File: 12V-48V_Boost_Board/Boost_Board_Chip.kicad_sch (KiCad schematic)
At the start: 22 parts, among them Q1 100V

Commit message: Implemented feedback from request
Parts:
- L1: footprint Inductor_SMD:L_0805_2012Metric_Pad1.05x1.20mm_HandSolder -> Library:WE-HCF_SMD_HIGH-CURRENT_INDUCTOR
- R4: value 1000Ω -> 1kΩ
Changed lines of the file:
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@@
 	(wire
 		(pts
-			(xy 30.48 60.96) (xy 43.18 60.96)
+			(xy 38.1 60.96) (xy 43.18 60.96)
 		)
 		(stroke
@@
 	(wire
 		(pts
-			(xy 30.48 60.96) (xy 30.48 110.49)
-		)
-		(stroke
-			(width 0)
-			(type default)
-		)
-	)
-	(wire
-		(pts
 			(xy 152.4 121.92) (xy 152.4 128.27)
 		)
@@
 	(wire
 		(pts
-			(xy 265.43 60.96) (xy 265.43 110.49)
-		)
-		(stroke
-			(width 0)
-			(type default)
-		)
-	)
-	(wire
-		(pts
 			(xy 166.37 93.98) (xy 166.37 124.46)
 		)
@@
 	(wire
 		(pts
-			(xy 246.38 60.96) (xy 265.43 60.96)
+			(xy 246.38 60.96) (xy 254 60.96)
 		)
 		(stroke
@@
 	(hierarchical_label "12V_INPUT"
 		(shape output)
-		(at 30.48 110.49 180)
+		(at 38.1 60.96 180)
 		(fields_autoplaced yes)
 		(effects
@@
 	(hierarchical_label "48V_OUTPUT"
 		(shape input)
-		(at 265.43 110.49 0)
+		(at 254 60.96 0)
 		(fields_autoplaced yes)
 		(effects
@@
 			)
 		)
-		(property "Datasheet" ""
+		(property "Datasheet" "https://www.ti.com/lit/ds/symlink/lm5156h.pdf?ts=1732642562165"
 			(at 113.03 85.09 0)
 			(effects
@@
 			)
 		)
-		(property "Datasheet" "~"
+		(property "Datasheet" "https://www.onsemi.com/pdf/datasheet/fdws86068-f085-d.pdf"
 			(at 161.29 73.66 0)
 			(effects
@@
 			)
 		)
-		(property "Description" "Depletion-mode N-channel MOSFET, drain/gate/source"
+		(property "Description" "FDWS86068-F085"
 			(at 161.29 73.66 0)
 			(effects
@@
 			)
 		)
-		(property "Footprint" "Inductor_SMD:L_0805_2012Metric_Pad1.05x1.20mm_HandSolder"
+		(property "Footprint" "Library:WE-HCF_SMD_HIGH-CURRENT_INDUCTOR"
 			(at 113.03 60.96 0)
 			(effects
@@
 			)
 		)
-		(property "Datasheet" "~"
+		(property "Datasheet" "https://www.we-online.com/components/products/datasheet/7443640680.pdf"
 			(at 113.03 60.96 0)
 			(effects
@@
 			)
 		)
-		(property "Description" "Inductor"
+		(property "Description" "7443640680 Inductor from we-online"
 			(at 113.03 60.96 0)
 			(effects
@@
 			)
 		)
-		(property "Value" "1000Ω"
+		(property "Value" "1kΩ"
 			(at 152.4 86.36 90)
 			(effects
@@
 			)
 		)
-		(property "Datasheet" "~"
+		(property "Datasheet" "https://www.onsemi.com/pdf/datasheet/mbr1080-d.pdf"
 			(at 200.66 60.96 0)
 			(effects
@@
 			)
 		)
-		(property "Description" "Diode"
+		(property "Description" "MBR10100G"
 			(at 200.66 60.96 0)
 			(effects

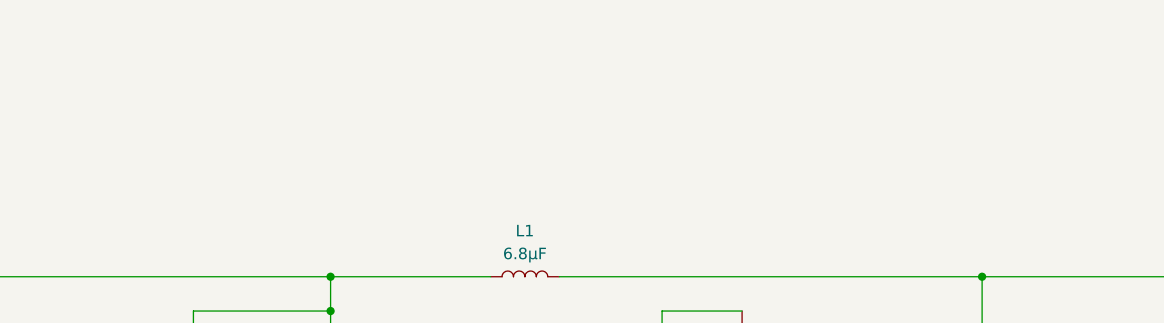
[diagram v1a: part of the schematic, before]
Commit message: Changed small text on boost board to make link more accessible
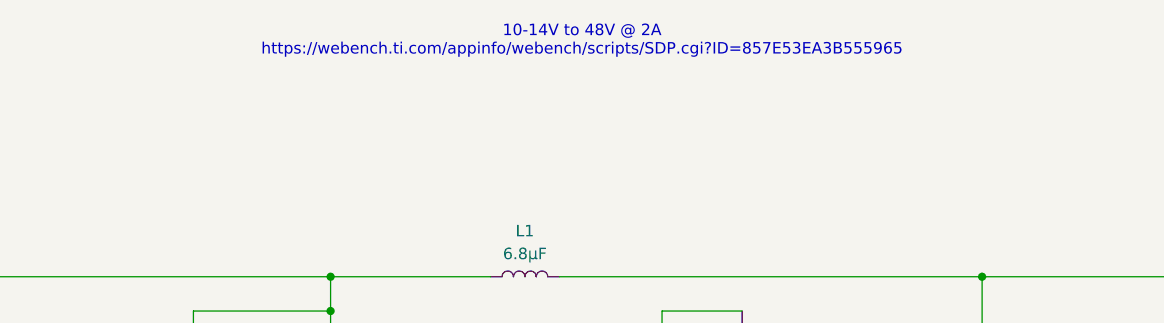
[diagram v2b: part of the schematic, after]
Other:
- note added: "10-14V to 48V @ 2A https://webench.ti.com/appinfo/webench/scripts/SDP.cgi?ID=857E53EA3B555965"
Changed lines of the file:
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@@
+		)
+	)
+	(text "10-14V to 48V @ 2A\nhttps://webench.ti.com/appinfo/webench/scripts/SDP.cgi?ID=857E53EA3B555965"
+		(exclude_from_sim no)
+		(at 119.38 34.798 0)
+		(effects
+			(font
+				(size 1.27 1.27)
+			)
 		)
 	)

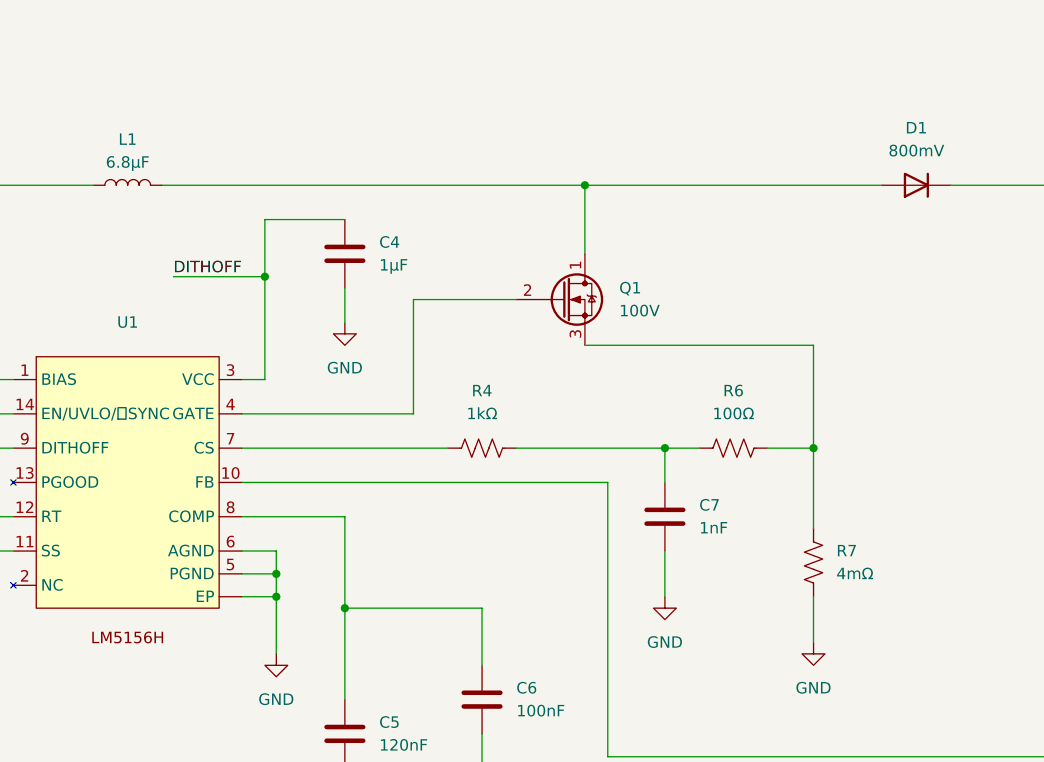
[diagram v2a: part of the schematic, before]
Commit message: Changed mosfet symbol to be more accurate to proposed mosfet
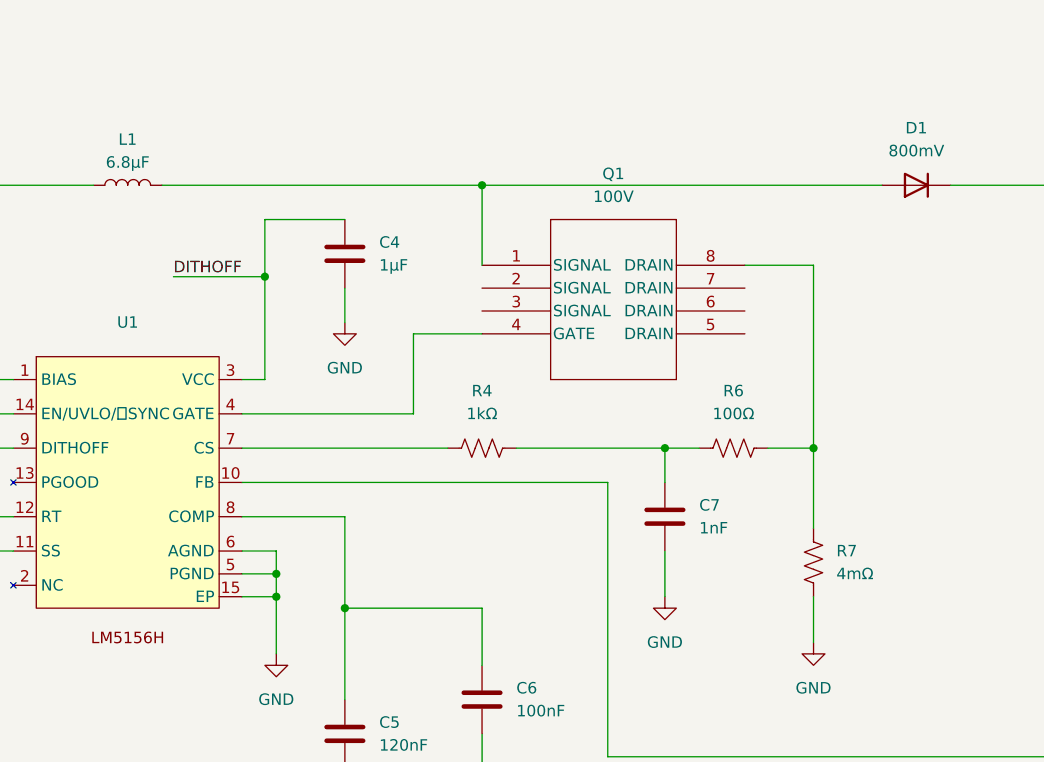
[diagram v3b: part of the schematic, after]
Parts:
- Q1: symbol Device:Q_NMOS_Depletion_DGS -> Boost_Board_Symbols:FDWS86068-F085
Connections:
- net GND: now also U1.15 (EP); no longer U1. (EP)
- net at U1.4 (GATE): now also Q1.4 (GATE); no longer Q1.2 (G)
- net at R6.1, R7.1: now also Q1.8 (DRAIN); no longer Q1.3 (S)
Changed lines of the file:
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@@
-	)
-	(junction
-		(at 163.83 60.96)
-		(diameter 0)
-		(color 0 0 0 0)
 	)
 	(junction
@@
 		(color 0 0 0 0)
 	)
+	(junction
+		(at 152.4 60.96)
+		(diameter 0)
+		(color 0 0 0 0)
+	)
 	(wire
 		(pts
@@
 	(wire
 		(pts
-			(xy 144.78 86.36) (xy 144.78 73.66)
-		)
-		(stroke
-			(width 0)
-			(type default)
-		)
-	)
-	(wire
-		(pts
 			(xy 172.72 90.17) (xy 172.72 93.98)
 		)
@@
 	(wire
 		(pts
+			(xy 152.4 60.96) (xy 152.4 69.85)
+		)
+		(stroke
+			(width 0)
+			(type default)
+		)
+	)
+	(wire
+		(pts
 			(xy 43.18 60.96) (xy 52.07 60.96)
 		)
@@
 	(wire
 		(pts
-			(xy 116.84 60.96) (xy 163.83 60.96)
+			(xy 116.84 60.96) (xy 152.4 60.96)
 		)
 		(stroke
@@
 	(wire
 		(pts
-			(xy 189.23 78.74) (xy 189.23 90.17)
+			(xy 189.23 69.85) (xy 189.23 90.17)
 		)
 		(stroke
@@
 	(wire
 		(pts
-			(xy 163.83 60.96) (xy 196.85 60.96)
-		)
-		(stroke
-			(width 0)
-			(type default)
-		)
-	)
-	(wire
-		(pts
 			(xy 246.38 127) (xy 246.38 137.16)
 		)
@@
 	(wire
 		(pts
+			(xy 144.78 77.47) (xy 152.4 77.47)
+		)
+		(stroke
+			(width 0)
+			(type default)
+		)
+	)
+	(wire
+		(pts
 			(xy 128.27 82.55) (xy 125.73 82.55)
 		)
@@
 	(wire
 		(pts
+			(xy 152.4 60.96) (xy 196.85 60.96)
+		)
+		(stroke
+			(width 0)
+			(type default)
+		)
+	)
+	(wire
+		(pts
 			(xy 152.4 135.89) (xy 152.4 140.97)
 		)
@@
 	(wire
 		(pts
-			(xy 163.83 78.74) (xy 189.23 78.74)
-		)
-		(stroke
-			(width 0)
-			(type default)
-		)
-	)
-	(wire
-		(pts
 			(xy 137.16 107.95) (xy 137.16 118.11)
 		)
@@
 	(wire
 		(pts
-			(xy 163.83 60.96) (xy 163.83 68.58)
-		)
-		(stroke
-			(width 0)
-			(type default)
-		)
-	)
-	(wire
-		(pts
 			(xy 152.4 121.92) (xy 152.4 128.27)
 		)
@@
 	(wire
 		(pts
-			(xy 144.78 73.66) (xy 156.21 73.66)
-		)
-		(stroke
-			(width 0)
-			(type default)
-		)
-	)
-	(wire
-		(pts
 			(xy 91.44 64.77) (xy 91.44 60.96)
 		)
@@
 	(wire
 		(pts
+			(xy 181.61 69.85) (xy 189.23 69.85)
+		)
+		(stroke
+			(width 0)
+			(type default)
+		)
+	)
+	(wire
+		(pts
 			(xy 246.38 60.96) (xy 254 60.96)
 		)
@@
 		(pts
 			(xy 125.73 86.36) (xy 144.78 86.36)
+		)
+		(stroke
+			(width 0)
+			(type default)
+		)
+	)
+	(wire
+		(pts
+			(xy 144.78 86.36) (xy 144.78 77.47)
 		)
 		(stroke
@@
 		(pin "7"
 		)
-		(pin ""
+		(pin "15"
 		)
 		(instances
@@
 	)
 	(symbol
-		(lib_id "Device:Q_NMOS_Depletion_DGS")
-		(at 161.29 73.66 0)
+		(lib_id "Boost_Board_Symbols:FDWS86068-F085")
+		(at 167.64 73.66 0)
 		(unit 1)
 		(exclude_from_sim no)
@@
 		(fields_autoplaced yes)
 		(property "Reference" "Q1"
-			(at 167.64 72.3899 0)
-			(effects
-				(font
-					(size 1.27 1.27)
-				)
-				(justify left)
+			(at 167.005 59.69 0)
+			(effects
+				(font
+					(size 1.27 1.27)
+				)
 			)
 		)
 		(property "Value" "100V"
-			(at 167.64 74.9299 0)
-			(effects
-				(font
-					(size 1.27 1.27)
-				)
-				(justify left)
+			(at 167.005 62.23 0)
+			(effects
+				(font
+					(size 1.27 1.27)
+				)
 			)
 		)
 		(property "Footprint" "Library:Q1 Mosfet"
-			(at 161.29 73.66 0)
-			(effects
-				(font
-					(size 1.27 1.27)
-				)
-				(hide yes)
-			)
-		)
-		(property "Datasheet" "https://www.onsemi.com/pdf/datasheet/fdws86068-f085-d.pdf"
-			(at 161.29 73.66 0)
-			(effects
-				(font
-					(size 1.27 1.27)
+			(at 167.64 85.344 0)
+			(effects
+				(font
+					(size 1.27 1.27)
+					(italic yes)
+				)
+				(hide yes)
+			)
+		)
+		(property "Datasheet" "FDWS86068-F085"
+			(at 167.64 88.9 0)
+			(effects
+				(font
+					(size 1.27 1.27)
+					(italic yes)
 				)
 				(hide yes)
@@
 		)
 		(property "Description" "FDWS86068-F085"
-			(at 161.29 73.66 0)
+			(at 144.78 69.85 0)
 			(effects
 				(font
@@
 		)
 		(property "Sim.Device" "NMOS"
-			(at 161.29 73.66 0)
+			(at 167.64 73.66 0)
 			(effects
 				(font
@@
 		)
 		(property "Sim.Type" "VDMOS"
-			(at 161.29 73.66 0)
+			(at 167.64 73.66 0)
 			(effects
 				(font
@@
 		)
 		(property "Sim.Pins" "1=D 2=G 3=S"
-			(at 161.29 73.66 0)
+			(at 167.64 73.66 0)
 			(effects
 				(font
@@
 		)
 		(property "Sim.Params" "vto=100"
-			(at 161.29 73.66 0)
+			(at 167.64 73.66 0)
 			(effects
 				(font
@@
 		(pin "3"
 		)
+		(pin "4"
+		)
+		(pin "5"
+		)
+		(pin "6"
+		)
+		(pin "7"
+		)
+		(pin "8"
+		)
 		(instances

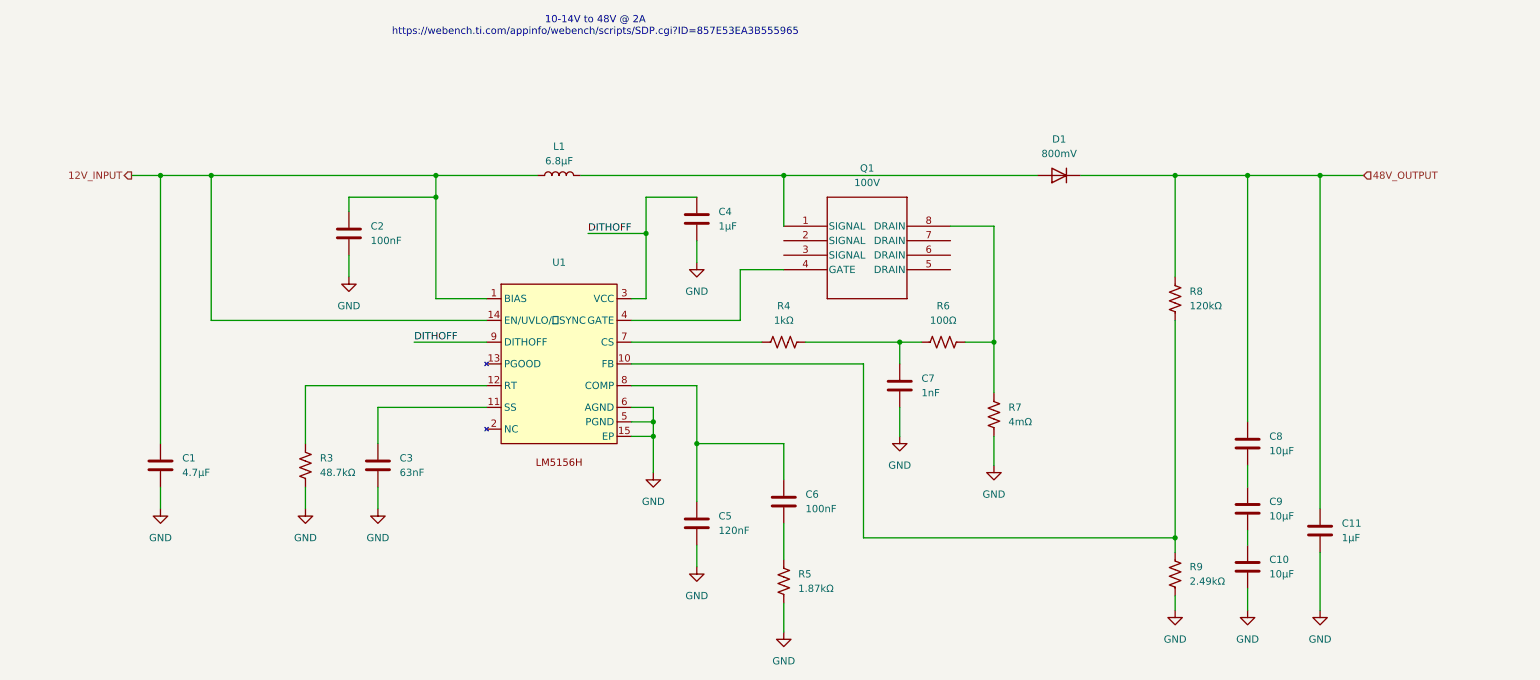
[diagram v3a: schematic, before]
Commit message: Implemented feedback from request V2
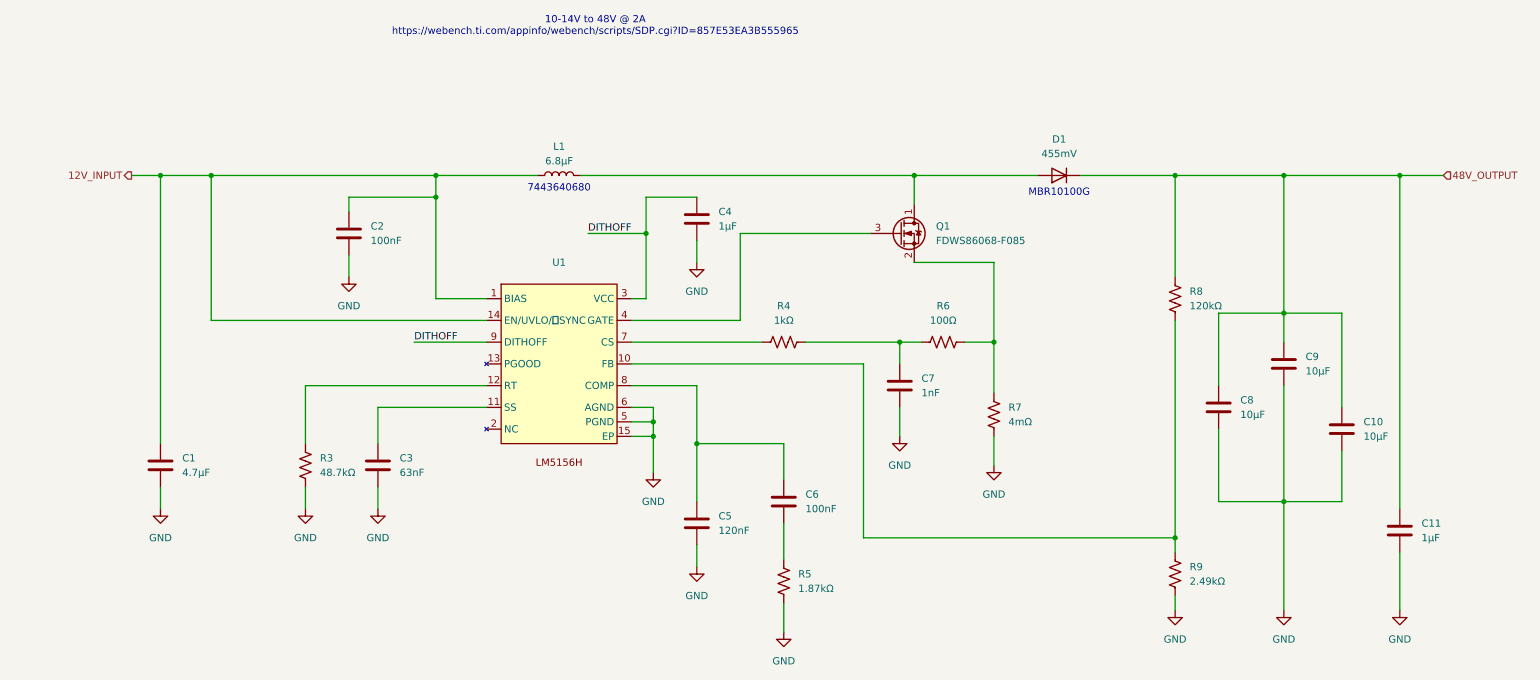
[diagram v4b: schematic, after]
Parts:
- removed Q1: 100V, Library:Q1 Mosfet, symbol Boost_Board_Symbols:FDWS86068-F085
- added Q1: FDWS86068-F085, Library:Q1 Mosfet, symbol Device:Q_NMOS_DSG
- D1: value 800mV -> 455mV; footprint Library:TO-220-2 -> Library:D2PAK_STM-M
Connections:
- net 48V_OUTPUT: now also C10.1, C9.1
- net GND: now also C8.2, C9.2
- net at U1.4 (GATE): now also Q1.3 (G)
- net at D1.2 (A), L1.2: now also Q1.1 (D)
- net at R6.1, R7.1: now also Q1.2 (S)
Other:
- note added: "7443640680"
- note added: "MBR10100G"
- moved on the sheet: C10, C11, C8, C9

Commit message: Implemented feedback from review V3
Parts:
- added C1: 4.7µF, Capacitor_SMD:C_0805_2012Metric_Pad1.18x1.45mm_HandSolder, symbol Device:C
- D1: footprint Library:D2PAK_STM-M -> 12/48 boost:D2PAK_STM-M
- L1: footprint Library:WE-HCF_SMD_HIGH-CURRENT_INDUCTOR -> 12/48 boost:WE-HCF_SMD_HIGH-CURRENT_INDUCTOR
- Q1: footprint Library:Q1 Mosfet -> 12/48 boost:Q1 Mosfet
- U1: footprint Library:LM5156H -> 12/48 boost:LM5156H
- renumbered C9 to C10, C10 to C11, C11 to C12, C1 to C2, C2 to C3, C3 to C4, C4 to C5, C5 to C6, C6 to C7, C7 to C8, C8 to C9
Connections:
- net 12V_INPUT: now also C1.1
- net GND: now also C1.2
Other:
- moved on the sheet: C2
